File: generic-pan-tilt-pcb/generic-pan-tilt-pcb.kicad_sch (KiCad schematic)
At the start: 29 parts, among them J1 B4P-VH-FB-B, J10 USB4115-03-C, J2 NC5MAV, J3 NC5FAV, J4 Conn_01x03, J5 BM03B-SRSS-TB, J6 Conn_01x03, J7 BM03B-SRSS-TB, J8 B12B-PH-SM4-TB, J9 B12B-PH-SM4-TB, SW1 PTS 647 SK70 SMTR2 LFS, SW2 PTS 647 SK70 SMTR2 LFS

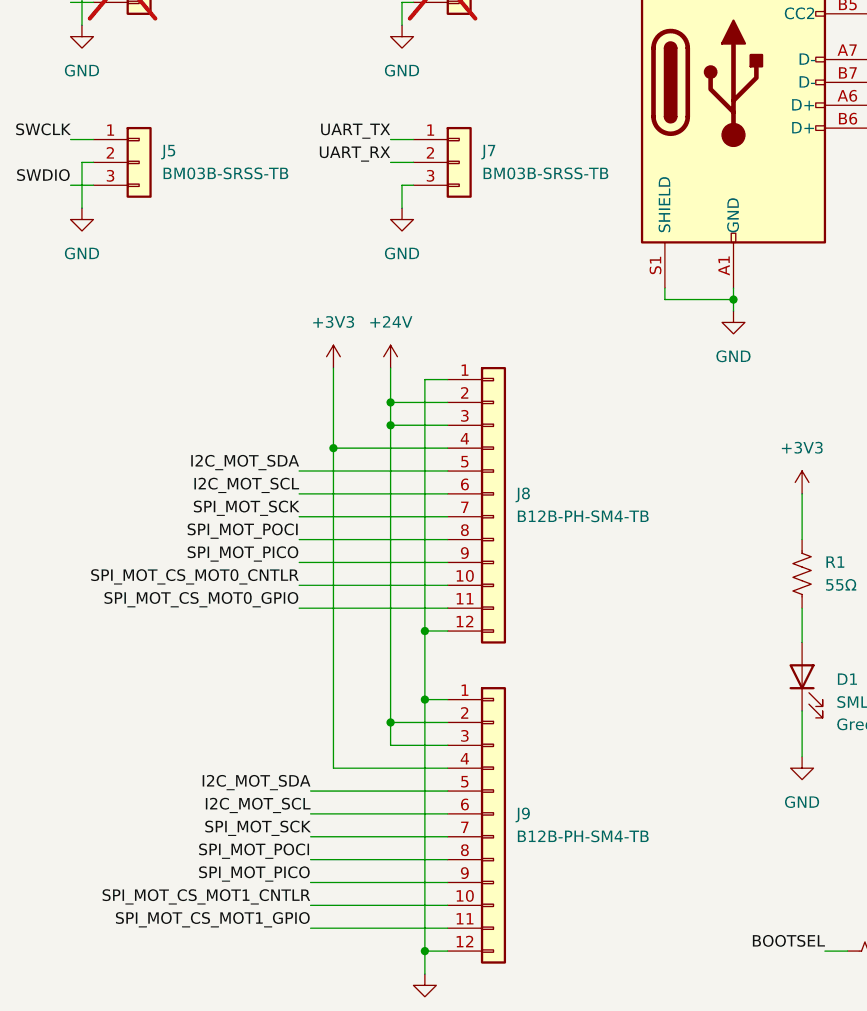
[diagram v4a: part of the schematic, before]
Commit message: more pcb, kicost maf digikey mouser
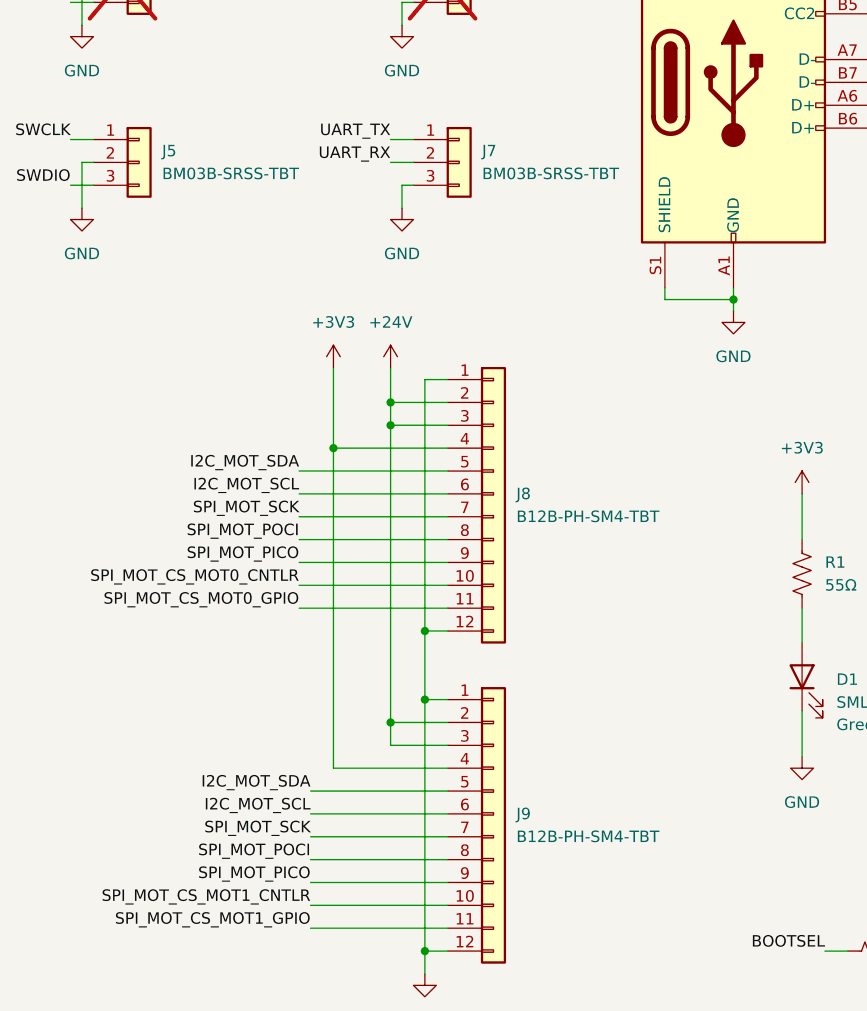
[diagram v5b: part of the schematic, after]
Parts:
- D1: digikey# (none) -> 846-SML-E12M8WT86CT-ND; manf# (none) -> SML-E12M8WT86; mouser# (none) -> 755-SML-E12M8WT86
- D2: digikey# (none) -> 846-SML-E12V8WT86CT-ND; manf# (none) -> SML-E12V8WT86; mouser# (none) -> 755-SML-E12V8WT86
- J1: digikey# (none) -> 455-B4P-VH-FB-B-ND
- J10: digikey# (none) -> 2073-USB4115-03-CCT-ND; manf# (none) -> USB4115-03-C; mouser# (none) -> 640-USB4115-03-C
- J2: manf# (none) -> NC5MAV; mouser# (none) -> 568-NC5MAV
- J3: manf# (none) -> NC5FAV; mouser# (none) -> 568-NC5FAV
- J5, J7: value BM03B-SRSS-TB -> BM03B-SRSS-TBT; digikey# (none) -> 455-BM03B-SRSS-TBTCT-ND
- J8, J9: value B12B-PH-SM4-TB -> B12B-PH-SM4-TBT; digikey# (none) -> 455-B12B-PH-SM4-TBTCT-ND
- SW1, SW2: digikey# (none) -> PTS647SK70SMTR2LFSCT-ND; manf# (none) -> PTS 647 SK70 SMTR2 LFS; mouser# (none) -> 611-PTS647SK70SMTR2L

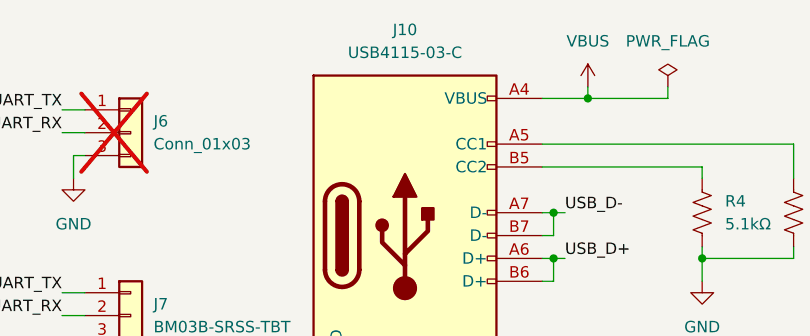
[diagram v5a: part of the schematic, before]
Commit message: mostly done with rp2040, horizontal usb
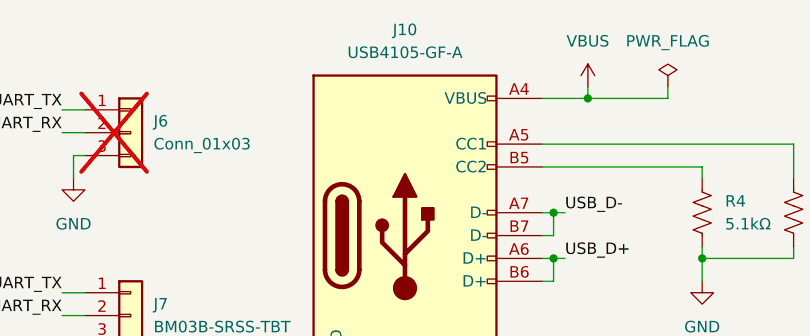
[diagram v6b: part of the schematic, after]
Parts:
- J10: value USB4115-03-C -> USB4105-GF-A; footprint Connector_USB:USB_C_Receptacle_GCT_USB4115-03-C -> USB_C_Receptacle_GCT_USB4105-xx-A_16P_TopMnt_Horizontal; digikey# 2073-USB4115-03-CCT-ND -> 2073-USB4105-GF-ACT-ND; manf# USB4115-03-C -> USB4105-GF-A; mouser# 640-USB4115-03-C -> 640-USB4105-GF-A
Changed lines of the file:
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@@
 			)
 		)
-		(property "Value" "USB4115-03-C"
+		(property "Value" "USB4105-GF-A"
 			(at 213.36 17.78 0)
 			(effects
@@
 			)
 		)
-		(property "Footprint" "Connector_USB:USB_C_Receptacle_GCT_USB4115-03-C"
+		(property "Footprint" "USB_C_Receptacle_GCT_USB4105-xx-A_16P_TopMnt_Horizontal"
 			(at 217.17 38.1 0)
 			(effects
@@
 			)
 		)
-		(property "manf#" "USB4115-03-C"
+		(property "manf#" "USB4105-GF-A"
 			(at 213.36 38.1 0)
 			(effects
@@
 			)
 		)
-		(property "digikey#" "2073-USB4115-03-CCT-ND"
+		(property "digikey#" "2073-USB4105-GF-ACT-ND"
 			(at 213.36 38.1 0)
 			(effects
@@
 			)
 		)
-		(property "mouser#" "640-USB4115-03-C"
+		(property "mouser#" "640-USB4105-GF-A"
 			(at 213.36 38.1 0)
 			(effects

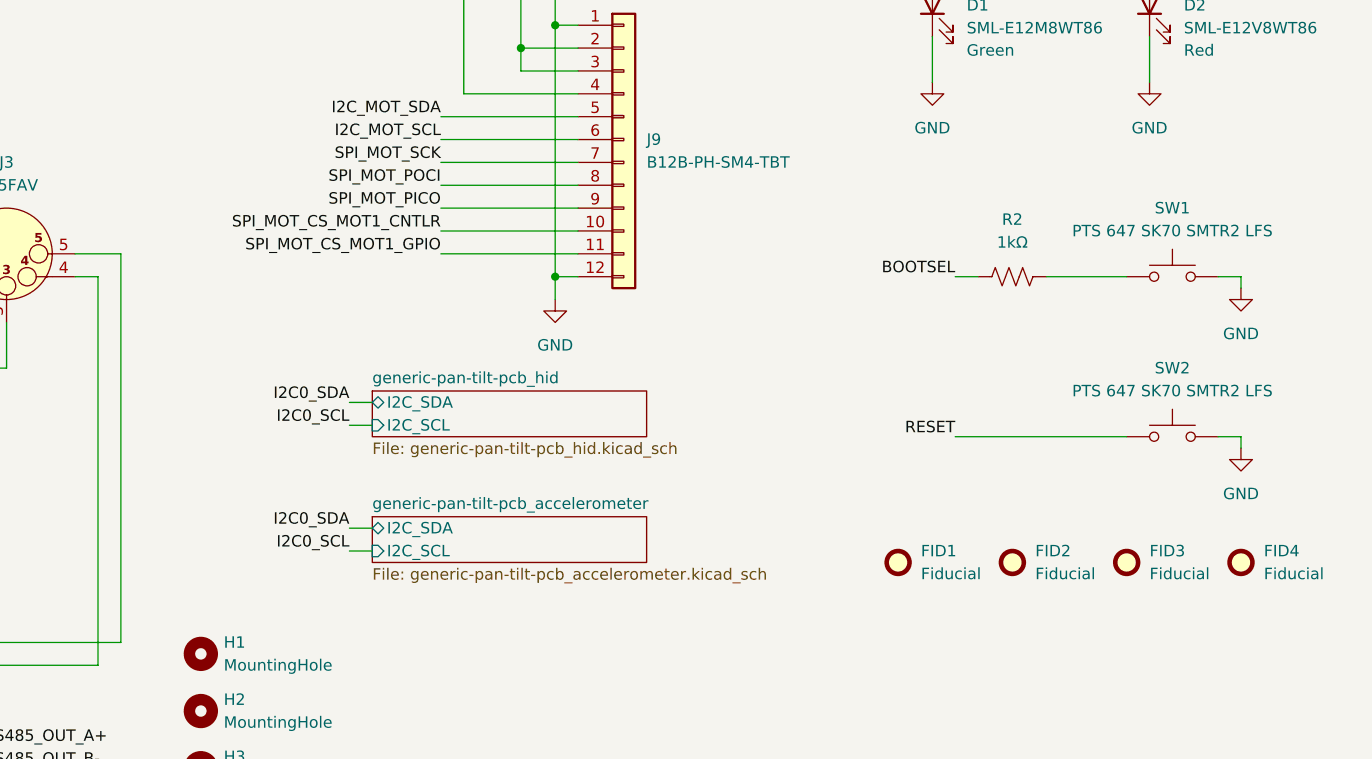
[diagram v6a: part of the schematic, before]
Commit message: add more fiducials
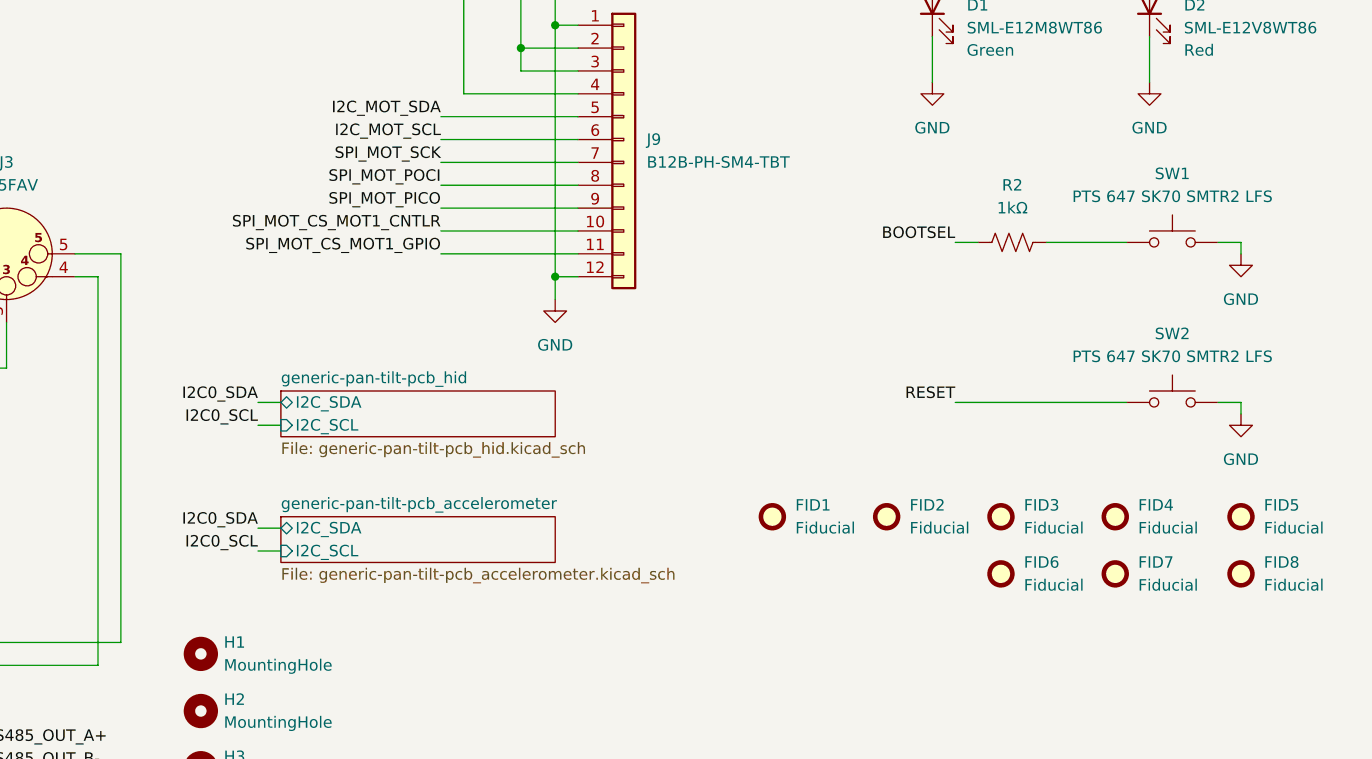
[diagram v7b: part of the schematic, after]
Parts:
- added FID5, FID6, FID7, FID8: Fiducial, Fiducial:Fiducial_0.5mm_Mask1mm, symbol Mechanical:Fiducial
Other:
- moved on the sheet: FID1, FID2, FID3, FID4, R2, SW1, SW2

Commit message: routing done, add oshw and license
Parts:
- added SYM1: Logo_Open_Hardware_Small, Symbol:OSHW-Logo2_7.3x6mm_SilkScreen, symbol Graphic:Logo_Open_Hardware_Small
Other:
- moved on the sheet: FID1, FID2, FID3, FID4, FID5, FID6, FID7, FID8
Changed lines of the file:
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@@
 		(company "Responsive Environments, MIT Media Lab")
 		(comment 1 "Perry Naseck")
+		(comment 2 "https://github.com/mitmedialab/generic-pan-tilt-pcb/")
+		(comment 3 "Licensed under CERN-OHL-P v2 or later")
+		(comment 4 "© MIT Media Lab 2024")
+		(comment 5 "This source describes Open Hardware and is licensed under the CERN-OHL-P v2")
+		(comment 6 "You may redistribute and modify this documentation and make products using it under the terms of the CERN-OHL-P v2 (https:/cern.ch/cern-ohl). This documentation is distributed WITHOUT ANY EXPRESS OR IMPLIED WARRANTY, INCLUDING OF MERCHANTABILITY, SATISFACTORY QUALITY AND FITNESS FOR A PARTICULAR PURPOSE. Please see the CERN-OHL-P v2 for applicable conditions")
 	)
 	(junction
@@
 	)
 	(symbol
+		(lib_id "Graphic:Logo_Open_Hardware_Small")
+		(at 260.35 165.1 0)
+		(unit 1)
+		(exclude_from_sim no)
+		(in_bom no)
+		(on_board yes)
+		(dnp no)
+		(fields_autoplaced yes)
+		(property "Reference" "SYM1"
+			(at 260.35 158.115 0)
+			(effects
+				(font
+					(size 1.27 1.27)
+				)
+				(hide yes)
+			)
+		)
+		(property "Value" "Logo_Open_Hardware_Small"
+			(at 260.35 170.815 0)
+			(effects
+				(font
+					(size 1.27 1.27)
+				)
+				(hide yes)
+			)
+		)
+		(property "Footprint" "Symbol:OSHW-Logo2_7.3x6mm_SilkScreen"
+			(at 260.35 165.1 0)
+			(effects
+				(font
+					(size 1.27 1.27)
+				)
+				(hide yes)
+			)
+		)
+		(property "Datasheet" "~"
+			(at 260.35 165.1 0)
+			(effects
+				(font
+					(size 1.27 1.27)
+				)
+				(hide yes)
+			)
+		)
+		(property "Description" "Open Hardware logo, small"
+			(at 260.35 165.1 0)
+			(effects
+				(font
+					(size 1.27 1.27)
+				)
+				(hide yes)
+			)
+		)
+		(property "Sim.Enable" "0"
+			(at 260.35 165.1 0)
+			(effects
+				(font
+					(size 1.27 1.27)
+				)
+				(hide yes)
+			)
+		)
+		(instances
+			(project ""
+				(path "/e3bbbe58-bf8f-42a8-8505-028de8235dc1"
+					(reference "SYM1")
+					(unit 1)
+				)
+			)
+		)
+	)
+	(symbol
 		(lib_id "power:PWR_FLAG")
 		(at 242.57 21.59 0)
@@
 	(symbol
 		(lib_id "Mechanical:Fiducial")
-		(at 215.9 161.29 0)
+		(at 203.2 161.29 0)
 		(unit 1)
 		(exclude_from_sim yes)
@@
 		(dnp no)
 		(property "Reference" "FID2"
-			(at 218.44 160.0199 0)
+			(at 205.74 160.0199 0)
 			(effects
 				(font
@@
 		)
 		(property "Value" "Fiducial"
-			(at 218.44 162.5599 0)
+			(at 205.74 162.5599 0)
 			(effects
 				(font
@@
 		)
 		(property "Footprint" "Fiducial:Fiducial_0.5mm_Mask1mm"
-			(at 215.9 161.29 0)
+			(at 203.2 161.29 0)
 			(effects
 				(font
@@
 		)
 		(property "Datasheet" "~"
-			(at 215.9 161.29 0)
+			(at 203.2 161.29 0)
 			(effects
 				(font
@@
 		)
 		(property "Description" "Fiducial Marker"
-			(at 215.9 161.29 0)
+			(at 203.2 161.29 0)
 			(effects
 				(font
@@
 	(symbol
 		(lib_id "Mechanical:Fiducial")
-		(at 241.3 167.64 0)
+		(at 228.6 167.64 0)
 		(unit 1)
 		(exclude_from_sim yes)
@@
 		(dnp no)
 		(property "Reference" "FID7"
-			(at 243.84 166.3699 0)
+			(at 231.14 166.3699 0)
 			(effects
 				(font
@@
 		)
 		(property "Value" "Fiducial"
-			(at 243.84 168.9099 0)
+			(at 231.14 168.9099 0)
 			(effects
 				(font
@@
 		)
 		(property "Footprint" "Fiducial:Fiducial_0.5mm_Mask1mm"
-			(at 241.3 167.64 0)
+			(at 228.6 167.64 0)
 			(effects
 				(font
@@
 		)
 		(property "Datasheet" "~"
-			(at 241.3 167.64 0)
+			(at 228.6 167.64 0)
 			(effects
 				(font
@@
 		)
 		(property "Description" "Fiducial Marker"
-			(at 241.3 167.64 0)
+			(at 228.6 167.64 0)
 			(effects
 				(font
@@
 	(symbol
 		(lib_id "Mechanical:Fiducial")
-		(at 255.27 161.29 0)
+		(at 242.57 161.29 0)
 		(unit 1)
 		(exclude_from_sim yes)
@@
 		(dnp no)
 		(property "Reference" "FID5"
-			(at 257.81 160.0199 0)
+			(at 245.11 160.0199 0)
 			(effects
 				(font
@@
 		)
 		(property "Value" "Fiducial"
-			(at 257.81 162.5599 0)
+			(at 245.11 162.5599 0)
 			(effects
 				(font
@@
 		)
 		(property "Footprint" "Fiducial:Fiducial_0.5mm_Mask1mm"
-			(at 255.27 161.29 0)
+			(at 242.57 161.29 0)
 			(effects
 				(font
@@
 		)
 		(property "Datasheet" "~"
-			(at 255.27 161.29 0)
+			(at 242.57 161.29 0)
 			(effects
 				(font
@@
 		)
 		(property "Description" "Fiducial Marker"
-			(at 255.27 161.29 0)
+			(at 242.57 161.29 0)
 			(effects
 				(font
@@
 	(symbol
 		(lib_id "Mechanical:Fiducial")
-		(at 255.27 167.64 0)
+		(at 242.57 167.64 0)
 		(unit 1)
 		(exclude_from_sim yes)
@@
 		(dnp no)
 		(property "Reference" "FID8"
-			(at 257.81 166.3699 0)
+			(at 245.11 166.3699 0)
 			(effects
 				(font
@@
 		)
 		(property "Value" "Fiducial"
-			(at 257.81 168.9099 0)
+			(at 245.11 168.9099 0)
 			(effects
 				(font
@@
 		)
 		(property "Footprint" "Fiducial:Fiducial_0.5mm_Mask1mm"
-			(at 255.27 167.64 0)
+			(at 242.57 167.64 0)
 			(effects
 				(font
@@
 		)
 		(property "Datasheet" "~"
-			(at 255.27 167.64 0)
+			(at 242.57 167.64 0)
 			(effects
 				(font
@@
 		)
 		(property "Description" "Fiducial Marker"
-			(at 255.27 167.64 0)
+			(at 242.57 167.64 0)
 			(effects
 				(font
@@
 	(symbol
 		(lib_id "Mechanical:Fiducial")
-		(at 203.2 161.29 0)
+		(at 190.5 161.29 0)
 		(unit 1)
 		(exclude_from_sim yes)
@@
 		(dnp no)
 		(property "Reference" "FID1"
-			(at 205.74 160.0199 0)
+			(at 193.04 160.0199 0)
 			(effects
 				(font
@@
 		)
 		(property "Value" "Fiducial"
-			(at 205.74 162.5599 0)
+			(at 193.04 162.5599 0)
 			(effects
 				(font
@@
 		)
 		(property "Footprint" "Fiducial:Fiducial_0.5mm_Mask1mm"
-			(at 203.2 161.29 0)
+			(at 190.5 161.29 0)
 			(effects
 				(font
@@
 		)
 		(property "Datasheet" "~"
-			(at 203.2 161.29 0)
+			(at 190.5 161.29 0)
 			(effects
 				(font
@@
 		)
 		(property "Description" "Fiducial Marker"
-			(at 203.2 161.29 0)
+			(at 190.5 161.29 0)
 			(effects
 				(font
@@
 	(symbol
 		(lib_id "Mechanical:Fiducial")
-		(at 228.6 161.29 0)
+		(at 215.9 161.29 0)
 		(unit 1)
 		(exclude_from_sim yes)
@@
 		(dnp no)
 		(property "Reference" "FID3"
-			(at 231.14 160.0199 0)
+			(at 218.44 160.0199 0)
 			(effects
 				(font
@@
 		)
 		(property "Value" "Fiducial"
-			(at 231.14 162.5599 0)
+			(at 218.44 162.5599 0)
 			(effects
 				(font
@@
 		)
 		(property "Footprint" "Fiducial:Fiducial_0.5mm_Mask1mm"
-			(at 228.6 161.29 0)
+			(at 215.9 161.29 0)
 			(effects
 				(font
@@
 		)
 		(property "Datasheet" "~"
-			(at 228.6 161.29 0)
+			(at 215.9 161.29 0)
 			(effects
 				(font
@@
 		)
 		(property "Description" "Fiducial Marker"
-			(at 228.6 161.29 0)
+			(at 215.9 161.29 0)
 			(effects
 				(font
@@
 	(symbol
 		(lib_id "Mechanical:Fiducial")
-		(at 241.3 161.29 0)
+		(at 228.6 161.29 0)
 		(unit 1)
 		(exclude_from_sim yes)
@@
 		(dnp no)
 		(property "Reference" "FID4"
-			(at 243.84 160.0199 0)
+			(at 231.14 160.0199 0)
 			(effects
 				(font
@@
 		)
 		(property "Value" "Fiducial"
-			(at 243.84 162.5599 0)
+			(at 231.14 162.5599 0)
 			(effects
 				(font
@@
 		)
 		(property "Footprint" "Fiducial:Fiducial_0.5mm_Mask1mm"
-			(at 241.3 161.29 0)
+			(at 228.6 161.29 0)
 			(effects
 				(font
@@
 		)
 		(property "Datasheet" "~"
-			(at 241.3 161.29 0)
+			(at 228.6 161.29 0)
 			(effects
 				(font
@@
 		)
 		(property "Description" "Fiducial Marker"
-			(at 241.3 161.29 0)
+			(at 228.6 161.29 0)
 			(effects
 				(font
@@
 	(symbol
 		(lib_id "Mechanical:Fiducial")
-		(at 228.6 167.64 0)
+		(at 215.9 167.64 0)
 		(unit 1)
 		(exclude_from_sim yes)
@@
 		(dnp no)
 		(property "Reference" "FID6"
-			(at 231.14 166.3699 0)
+			(at 218.44 166.3699 0)
 			(effects
 				(font
@@
 		)
 		(property "Value" "Fiducial"
-			(at 231.14 168.9099 0)
+			(at 218.44 168.9099 0)
 			(effects
 				(font
@@
 		)
 		(property "Footprint" "Fiducial:Fiducial_0.5mm_Mask1mm"
-			(at 228.6 167.64 0)
+			(at 215.9 167.64 0)
 			(effects
 				(font
@@
 		)
 		(property "Datasheet" "~"
-			(at 228.6 167.64 0)
+			(at 215.9 167.64 0)
 			(effects
 				(font
@@
 		)
 		(property "Description" "Fiducial Marker"
-			(at 228.6 167.64 0)
+			(at 215.9 167.64 0)
 			(effects
 				(font
